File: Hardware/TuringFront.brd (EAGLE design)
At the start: 107 x 49.5 mm, 73 parts, among them T1 2N3904, U1 TL074_

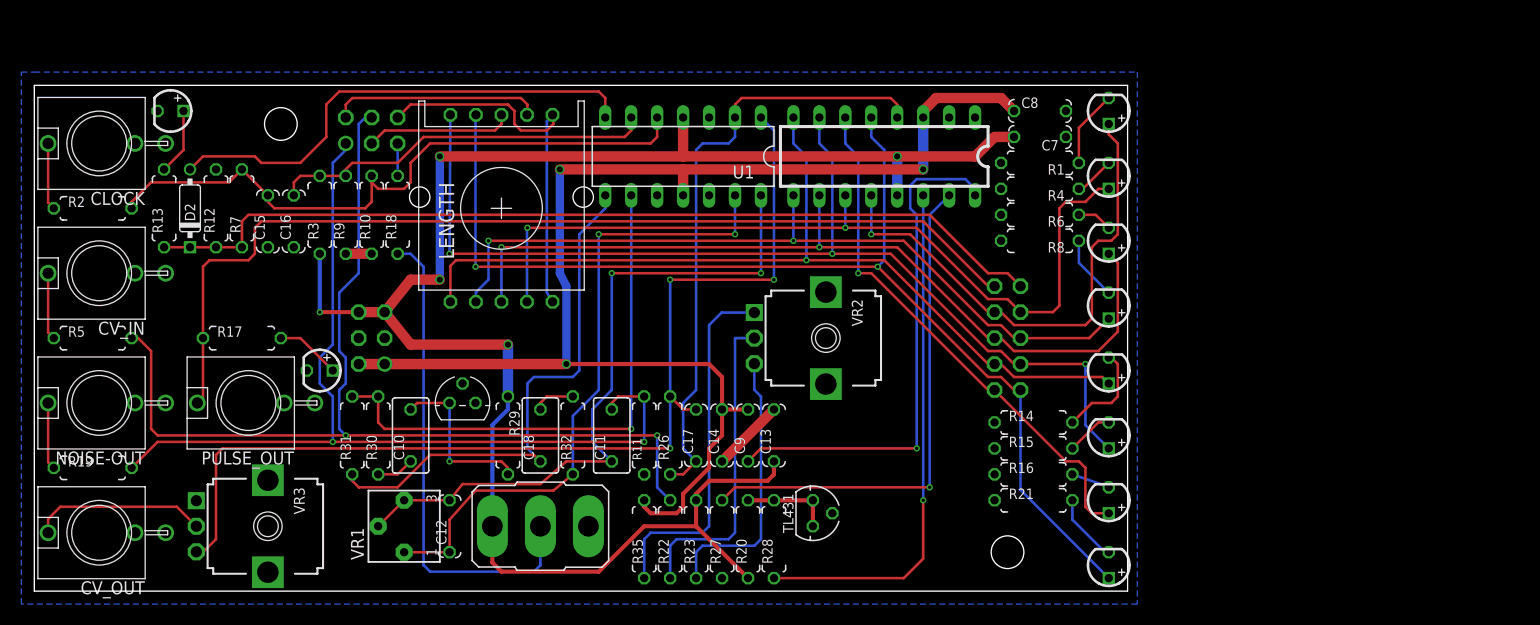
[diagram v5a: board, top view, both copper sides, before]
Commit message: cosmetic routing changes
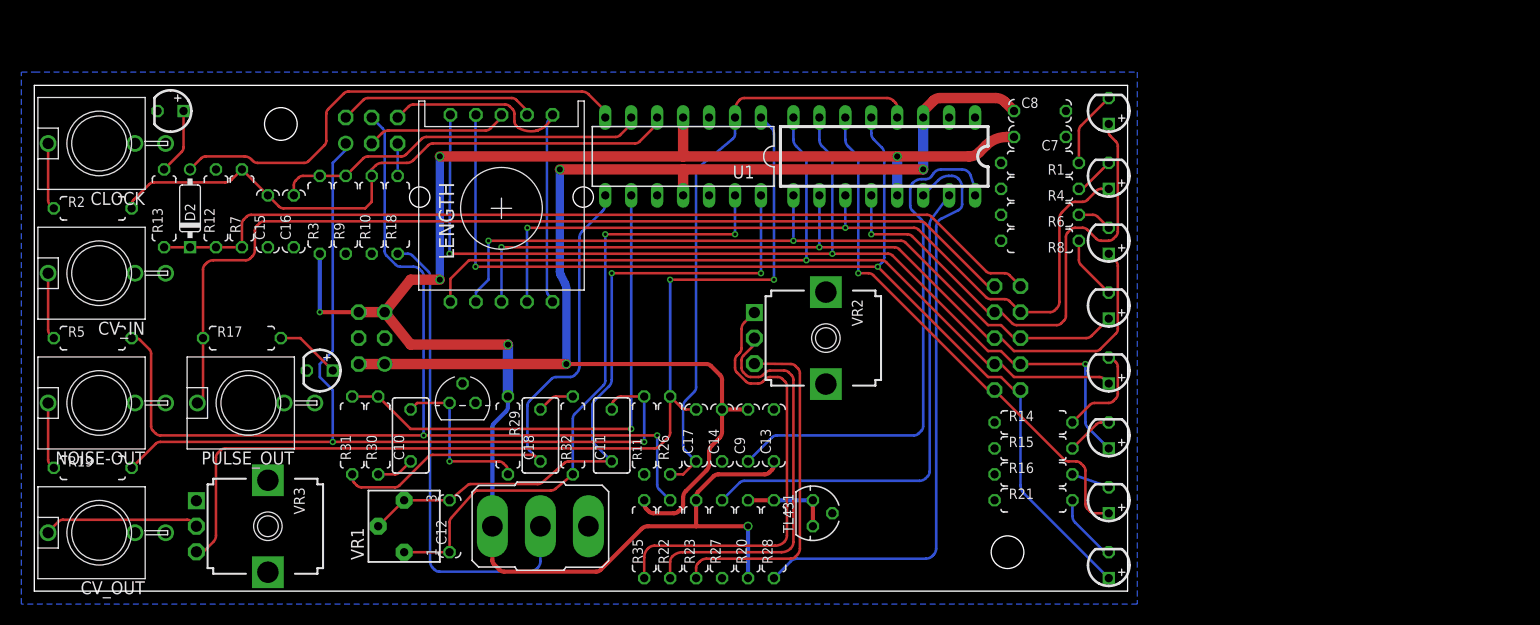
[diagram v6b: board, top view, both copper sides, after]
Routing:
- net GND_FRONT: track 9.72 -> 0.00 mm
- net N$43: track 31.0 -> 40.0 mm
- net N$48: track 35.3 -> 44.2 mm
- net N$26: track 51.0 -> 58.9 mm, vias 1 -> 0
- net N$47: track 26.9 -> 34.2 mm
- net N$5: track 64.2 -> 60.5 mm
- net +12V_FRONT: track 173.4 -> 175.3 mm, vias 5 -> 6
- net N$39: track 17.1 -> 15.3 mm
- net N$13: track 59.8 -> 58.0 mm
- net N$22: track 52.8 -> 51.2 mm
- net N$21: track 53.0 -> 51.5 mm
- net B8_FRONT: track 50.6 -> 51.9 mm
- net STEP_16_FRONT: track 20.6 -> 19.4 mm
- net N$8: track 48.4 -> 47.3 mm
- net N$23: track 50.2 -> 49.1 mm, vias 1 -> 0
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
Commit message: Routing tweaks
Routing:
- net LOOP_CTRL_FRONT: track 100.6 -> 117.8 mm, vias 2 -> 1
- net B1_FRONT: track 110.4 -> 114.2 mm
- net +12V_FRONT: track 175.3 -> 173.6 mm, vias 6 -> 5
- net N$5: track 60.5 -> 59.0 mm
- net B2_FRONT: track 51.9 -> 51.0 mm

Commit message: StillTweaking
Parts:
- moved R8 31.3 mm to (85.7, 5.71)
- moved R6 30.1 mm to (85.7, 9.53)
- moved R4 29.0 mm to (85.7, 13.3)
- moved R1 27.8 mm to (85.7, 17.1)
- moved C8 4.07 mm to (101.0, 43.8), turned to 90 degrees
- moved U$2 1.27 mm to (84.5, 42.5)
- moved C7 0.90 mm to (97.8, 45.1), turned to 270 degrees
- moved U1 0.64 mm to (64.1, 42.5)
- moved R15 0.63 mm to (97.8, 14.6)
- moved R16 0.63 mm to (97.8, 12.1)
- moved R21 0.63 mm to (97.8, 9.53)
- moved C12 0.63 mm to (41.3, 6.35)
- moved R14 0.63 mm to (97.8, 17.1)
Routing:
- net N$30: track 7.52 -> 44.4 mm
- net N$31: track 3.97 -> 40.5 mm
- net N$32: track 3.40 -> 38.3 mm
- net N$33: track 6.25 -> 35.4 mm
- net NOISE_FRONT: track 90.4 -> 107.9 mm, vias 2 -> 0
- net LOOP_CTRL_FRONT: track 117.8 -> 104.6 mm
- net B2_FRONT: track 51.0 -> 55.5 mm
- net N$25: track 51.2 -> 47.4 mm
- net -12V_FRONT: track 130.2 -> 133.7 mm
- net B8_FRONT: track 51.9 -> 48.5 mm
- net N$23: track 49.1 -> 46.6 mm
- net B3_FRONT: track 103.2 -> 105.5 mm, vias 3 -> 2
- net N$34: track 9.66 -> 8.16 mm
- net +12V_FRONT: track 173.6 -> 175.0 mm
- net N$37: track 6.72 -> 7.78 mm
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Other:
- board text added: "Music Thing Modular Turing Machine Rev 4 Prototype 1 Front Board September 2015 CC-BY-SA"
- board text removed: "Music Thing Modular Turing Machine Rev 4 Prototype 2 July 2015 CC-BY-SA"
